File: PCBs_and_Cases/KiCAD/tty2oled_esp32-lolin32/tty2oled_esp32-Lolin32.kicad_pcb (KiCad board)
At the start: 2 copper layers, 35.6 x 99.7 mm, 25 parts

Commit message: Fixup of the Käseecke :)
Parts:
- removed the REF** at (158.8, 122.9) (x2)
- added REF**: PADS_0805, _my_footprints:PAD_0805, B.Cu at (158.8, 122.9)
- added REF**: PADS_0805, _my_footprints:PAD_0805, F.Cu at (158.8, 122.9)
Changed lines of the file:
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@@
   (general
     (thickness 1.6)
-    (drawings 38)
+    (drawings 37)
     (tracks 138)
     (zones 0)
@@
       (effects (font (size 1 1) (thickness 0.15)))
     )
+    (fp_line (start 1.27 40.64) (end 1.27 35.56) (layer F.SilkS) (width 0.15))
+    (fp_line (start 1.27 35.56) (end 8.89 35.56) (layer F.SilkS) (width 0.15))
+    (fp_line (start 8.89 35.56) (end 8.89 40.64) (layer F.SilkS) (width 0.15))
+    (fp_line (start -8.89 31.75) (end -3.81 31.75) (layer F.SilkS) (width 0.15))
+    (fp_line (start -3.81 31.75) (end -3.81 38.1) (layer F.SilkS) (width 0.15))
+    (fp_line (start -3.81 38.1) (end -8.89 38.1) (layer F.SilkS) (width 0.15))
+    (fp_line (start -8.89 38.1) (end -8.89 31.75) (layer F.SilkS) (width 0.15))
+    (fp_line (start -6.35 -11.43) (end -6.35 6.35) (layer F.SilkS) (width 0.15))
+    (fp_line (start -6.35 6.35) (end 11.43 6.35) (layer F.SilkS) (width 0.15))
+    (fp_line (start 11.43 6.35) (end 11.43 -11.43) (layer F.SilkS) (width 0.15))
+    (fp_line (start 11.43 -11.43) (end -6.35 -11.43) (layer F.SilkS) (width 0.15))
+    (fp_line (start 15.24 -16.51) (end 15.24 39.37) (layer F.SilkS) (width 0.15))
+    (fp_line (start -7.62 -19.05) (end 12.7 -19.05) (layer F.SilkS) (width 0.15))
+    (fp_line (start 13.97 40.64) (end -8.89 40.64) (layer F.SilkS) (width 0.15))
+    (fp_line (start -8.89 40.64) (end -10.16 39.37) (layer F.SilkS) (width 0.15))
+    (fp_line (start -10.16 39.37) (end -10.16 -16.51) (layer F.SilkS) (width 0.15))
+    (fp_line (start 15.24 39.37) (end 13.97 40.64) (layer F.SilkS) (width 0.15))
+    (fp_line (start 12.7 -19.05) (end 15.24 -16.51) (layer F.SilkS) (width 0.15))
     (fp_line (start -10.16 -16.51) (end -7.62 -19.05) (layer F.SilkS) (width 0.15))
-    (fp_line (start 12.7 -19.05) (end 15.24 -16.51) (layer F.SilkS) (width 0.15))
-    (fp_line (start 15.24 39.37) (end 13.97 40.64) (layer F.SilkS) (width 0.15))
-    (fp_line (start -10.16 39.37) (end -10.16 -16.51) (layer F.SilkS) (width 0.15))
-    (fp_line (start -8.89 40.64) (end -10.16 39.37) (layer F.SilkS) (width 0.15))
-    (fp_line (start 13.97 40.64) (end -8.89 40.64) (layer F.SilkS) (width 0.15))
-    (fp_line (start -7.62 -19.05) (end 12.7 -19.05) (layer F.SilkS) (width 0.15))
-    (fp_line (start 15.24 -16.51) (end 15.24 39.37) (layer F.SilkS) (width 0.15))
-    (fp_line (start 11.43 -11.43) (end -6.35 -11.43) (layer F.SilkS) (width 0.15))
-    (fp_line (start 11.43 6.35) (end 11.43 -11.43) (layer F.SilkS) (width 0.15))
-    (fp_line (start -6.35 6.35) (end 11.43 6.35) (layer F.SilkS) (width 0.15))
-    (fp_line (start -6.35 -11.43) (end -6.35 6.35) (layer F.SilkS) (width 0.15))
-    (fp_line (start -8.89 38.1) (end -8.89 31.75) (layer F.SilkS) (width 0.15))
-    (fp_line (start -3.81 38.1) (end -8.89 38.1) (layer F.SilkS) (width 0.15))
-    (fp_line (start -3.81 31.75) (end -3.81 38.1) (layer F.SilkS) (width 0.15))
-    (fp_line (start -8.89 31.75) (end -3.81 31.75) (layer F.SilkS) (width 0.15))
-    (fp_line (start 8.89 35.56) (end 8.89 40.64) (layer F.SilkS) (width 0.15))
-    (fp_line (start 1.27 35.56) (end 8.89 35.56) (layer F.SilkS) (width 0.15))
-    (fp_line (start 1.27 40.64) (end 1.27 35.56) (layer F.SilkS) (width 0.15))
     (pad 15 thru_hole oval (at 13.97 38.1) (size 2.268 1.524) (drill 1) (layers *.Cu *.Mask))
     (pad 2 thru_hole oval (at 13.97 35.56) (size 2.268 1.524) (drill 1) (layers *.Cu *.Mask))
@@
       (effects (font (size 1 1) (thickness 0.15)) (justify mirror))
     )
+    (fp_line (start 4.35 1.8) (end -1.8 1.8) (layer B.CrtYd) (width 0.05))
+    (fp_line (start 4.35 -19.55) (end 4.35 1.8) (layer B.CrtYd) (width 0.05))
+    (fp_line (start -1.8 -19.55) (end 4.35 -19.55) (layer B.CrtYd) (width 0.05))
+    (fp_line (start -1.8 1.8) (end -1.8 -19.55) (layer B.CrtYd) (width 0.05))
+    (fp_line (start -1.33 1.33) (end 0 1.33) (layer B.SilkS) (width 0.12))
+    (fp_line (start -1.33 0) (end -1.33 1.33) (layer B.SilkS) (width 0.12))
+    (fp_line (start 1.27 1.33) (end 3.87 1.33) (layer B.SilkS) (width 0.12))
+    (fp_line (start 1.27 -1.27) (end 1.27 1.33) (layer B.SilkS) (width 0.12))
+    (fp_line (start -1.33 -1.27) (end 1.27 -1.27) (layer B.SilkS) (width 0.12))
+    (fp_line (start 3.87 1.33) (end 3.87 -19.11) (layer B.SilkS) (width 0.12))
+    (fp_line (start -1.33 -1.27) (end -1.33 -19.11) (layer B.SilkS) (width 0.12))
+    (fp_line (start -1.33 -19.11) (end 3.87 -19.11) (layer B.SilkS) (width 0.12))
+    (fp_line (start -1.27 0) (end 0 1.27) (layer B.Fab) (width 0.1))
+    (fp_line (start -1.27 -19.05) (end -1.27 0) (layer B.Fab) (width 0.1))
+    (fp_line (start 3.81 -19.05) (end -1.27 -19.05) (layer B.Fab) (width 0.1))
+    (fp_line (start 3.81 1.27) (end 3.81 -19.05) (layer B.Fab) (width 0.1))
     (fp_line (start 0 1.27) (end 3.81 1.27) (layer B.Fab) (width 0.1))
-    (fp_line (start 3.81 1.27) (end 3.81 -19.05) (layer B.Fab) (width 0.1))
-    (fp_line (start 3.81 -19.05) (end -1.27 -19.05) (layer B.Fab) (width 0.1))
-    (fp_line (start -1.27 -19.05) (end -1.27 0) (layer B.Fab) (width 0.1))
-    (fp_line (start -1.27 0) (end 0 1.27) (layer B.Fab) (width 0.1))
-    (fp_line (start -1.33 -19.11) (end 3.87 -19.11) (layer B.SilkS) (width 0.12))
-    (fp_line (start -1.33 -1.27) (end -1.33 -19.11) (layer B.SilkS) (width 0.12))
-    (fp_line (start 3.87 1.33) (end 3.87 -19.11) (layer B.SilkS) (width 0.12))
-    (fp_line (start -1.33 -1.27) (end 1.27 -1.27) (layer B.SilkS) (width 0.12))
-    (fp_line (start 1.27 -1.27) (end 1.27 1.33) (layer B.SilkS) (width 0.12))
-    (fp_line (start 1.27 1.33) (end 3.87 1.33) (layer B.SilkS) (width 0.12))
-    (fp_line (start -1.33 0) (end -1.33 1.33) (layer B.SilkS) (width 0.12))
-    (fp_line (start -1.33 1.33) (end 0 1.33) (layer B.SilkS) (width 0.12))
-    (fp_line (start -1.8 1.8) (end -1.8 -19.55) (layer B.CrtYd) (width 0.05))
-    (fp_line (start -1.8 -19.55) (end 4.35 -19.55) (layer B.CrtYd) (width 0.05))
-    (fp_line (start 4.35 -19.55) (end 4.35 1.8) (layer B.CrtYd) (width 0.05))
-    (fp_line (start 4.35 1.8) (end -1.8 1.8) (layer B.CrtYd) (width 0.05))
     (fp_text user %R (at 1.27 -8.89 180) (layer B.Fab)
       (effects (font (size 1 1) (thickness 0.15)) (justify mirror))
@@
   (gr_line (start 132.08 51.435) (end 132.08 151.13) (layer Edge.Cuts) (width 0.05))
   (gr_line (start 132.08 151.13) (end 167.64 151.13) (layer Edge.Cuts) (width 0.05))
-  (target plus (at 132.08 151.13) (size 5) (width 0.05) (layer Edge.Cuts))
   (gr_text 16 (at 161.544 53.975) (layer F.SilkS)
     (effects (font (size 1 1) (thickness 0.15)))

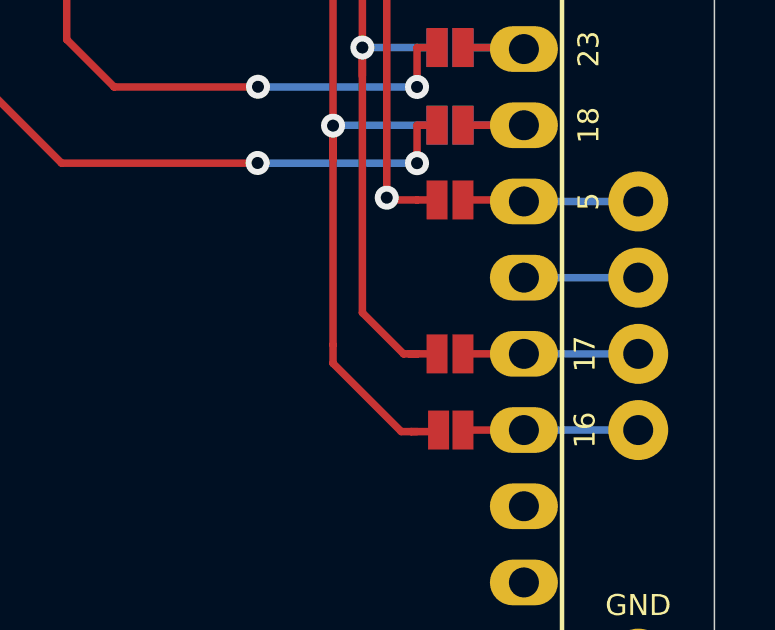
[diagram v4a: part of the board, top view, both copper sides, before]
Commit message: Fix of Pads for Pin#16 by 0.1mm
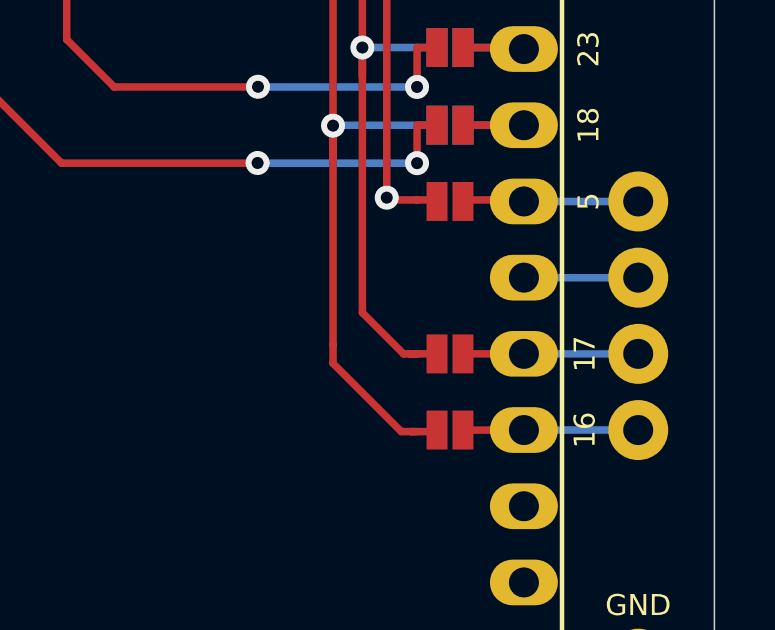
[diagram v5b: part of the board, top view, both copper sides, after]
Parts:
- removed the REF** at (158.8, 122.9) (x2)
- removed the REF** at (158.8, 128.0)
- removed the REF** at (158.9, 135.6)
- added REF**: PADS_0805, _my_footprints:PAD_0805, F.Cu at (158.8, 135.6)
- added REF**: PADS_0805, _my_footprints:PAD_0805, B.Cu at (158.8, 122.9)
- added REF**: PADS_0805, _my_footprints:PAD_0805, F.Cu at (158.8, 128.0)
- added REF**: PADS_0805, _my_footprints:PAD_0805, F.Cu at (158.8, 122.9)
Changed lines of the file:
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@@
     (uvia_drill 0.1)
   )
+  (module _my_footprints:PAD_0805 (layer F.Cu)
+    (at 158.8262 135.636)
+    (descr "Resistor SMD 0805, reflow soldering, Vishay (see dcrcw.pdf)")
+    (tags "resistor 0805")
+    (attr smd)
+    (fp_text reference REF** (at 0 -1.25) (layer F.SilkS) hide
+      (effects (font (size 1 1) (thickness 0.15)))
+    )
+    (fp_text value PADS_0805 (at 0 1.3) (layer F.Fab) hide
+      (effects (font (size 1 1) (thickness 0.15)))
+    )
+    (pad 1 smd rect (at -0.4318 0) (size 0.7 1.3) (layers F.Cu F.Paste F.Mask))
+    (pad 2 smd rect (at 0.4318 0) (size 0.7 1.3) (layers F.Cu F.Paste F.Mask))
+    (model ${KISYS3DMOD}/Resistors_SMD.3dshapes/R_0805.wrl
+      (at (xyz 0 0 0))
+      (scale (xyz 1 1 1))
+      (rotate (xyz 0 0 0))
+    )
+  )
+  (module _my_footprints:PAD_0805 (layer F.Cu)
+    (at 158.8262 128.016)
+    (descr "Resistor SMD 0805, reflow soldering, Vishay (see dcrcw.pdf)")
+    (tags "resistor 0805")
+    (attr smd)
+    (fp_text reference REF** (at 0 -1.25) (layer F.SilkS) hide
+      (effects (font (size 1 1) (thickness 0.15)))
+    )
+    (fp_text value PADS_0805 (at 0 1.3) (layer F.Fab) hide
+      (effects (font (size 1 1) (thickness 0.15)))
+    )
+    (pad 1 smd rect (at -0.4318 0) (size 0.7 1.3) (layers F.Cu F.Paste F.Mask))
+    (pad 2 smd rect (at 0.4318 0) (size 0.7 1.3) (layers F.Cu F.Paste F.Mask))
+    (model ${KISYS3DMOD}/Resistors_SMD.3dshapes/R_0805.wrl
+      (at (xyz 0 0 0))
+      (scale (xyz 1 1 1))
+      (rotate (xyz 0 0 0))
+    )
+  )
   (module Wire_Pads:SolderWirePad_single_0-8mmDrill (layer F.Cu)
     (at 165.1 143.256)
@@
   )
   (module _my_footprints:PAD_0805 (layer F.Cu)
-    (at 158.8262 127.9652)
-    (descr "Resistor SMD 0805, reflow soldering, Vishay (see dcrcw.pdf)")
-    (tags "resistor 0805")
-    (attr smd)
-    (fp_text reference REF** (at 0 -1.25) (layer F.SilkS) hide
-      (effects (font (size 1 1) (thickness 0.15)))
-    )
-    (fp_text value PADS_0805 (at 0 1.3) (layer F.Fab) hide
-      (effects (font (size 1 1) (thickness 0.15)))
-    )
-    (pad 2 smd rect (at 0.4318 0) (size 0.7 1.3) (layers F.Cu F.Paste F.Mask))
-    (pad 1 smd rect (at -0.4318 0) (size 0.7 1.3) (layers F.Cu F.Paste F.Mask))
-    (model ${KISYS3DMOD}/Resistors_SMD.3dshapes/R_0805.wrl
-      (at (xyz 0 0 0))
-      (scale (xyz 1 1 1))
-      (rotate (xyz 0 0 0))
-    )
-  )
-  (module _my_footprints:PAD_0805 (layer F.Cu)
     (at 158.8262 133.096)
     (descr "Resistor SMD 0805, reflow soldering, Vishay (see dcrcw.pdf)")
@@
     (model ${KISYS3DMOD}/Resistors_SMD.3dshapes/R_0805.wrl
       (at (xyz 0 0 0))
-      (scale (xyz 1 1 1))
-      (rotate (xyz 0 0 0))
-    )
-  )
-  (module _my_footprints:PAD_0805 (layer F.Cu)
-    (at 158.8516 135.636)
-    (descr "Resistor SMD 0805, reflow soldering, Vishay (see dcrcw.pdf)")
-    (tags "resistor 0805")
-    (attr smd)
-    (fp_text reference REF** (at 0 -1.65) (layer F.SilkS) hide
-      (effects (font (size 1 1) (thickness 0.15)))
-    )
-    (fp_text value PADS_0805 (at 0 1.75) (layer F.Fab) hide
-      (effects (font (size 1 1) (thickness 0.15)))
-    )
-    (pad 2 smd rect (at 0.4064 0) (size 0.7 1.3) (layers F.Cu F.Paste F.Mask))
-    (pad 1 smd rect (at -0.4064 0) (size 0.7 1.3) (layers F.Cu F.Paste F.Mask))
-    (model ${KISYS3DMOD}/Resistors_SMD.3dshapes/R_0805.wrl
-      (at (xyz 0 0 0))
